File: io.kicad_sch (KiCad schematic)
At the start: 107 parts, among them CN1 DF40C-50DP-0.4V, J1 USB3_A, J13 WiFi SMA, J14 BLE SMA, J15 WiFi PATCH, J16 BLE PATCH, J17 BLE PATCH, J18 WIFI PATCH, U1 FUSB302BMPX, U12 PI3USB302-AZBEX, U13 VL817-Q7, U14 SiP32508DT, U15 TS5A23157DGSR, U16 AMLGA7921, U17 SiP32508DT, U30 PE4259-63, U36 PE4259-63, U37 2450CF15A0100001E, U38 X4C60K1-20S, U39 XEC24P3-30G, U40 AD8317ACPZ-R7, U41 AD8317ACPZ-R7, U42 AD8317ACPZ-R7, U43 LM339D, U7 HD3SS3220RNHR, Y2 25 MHz

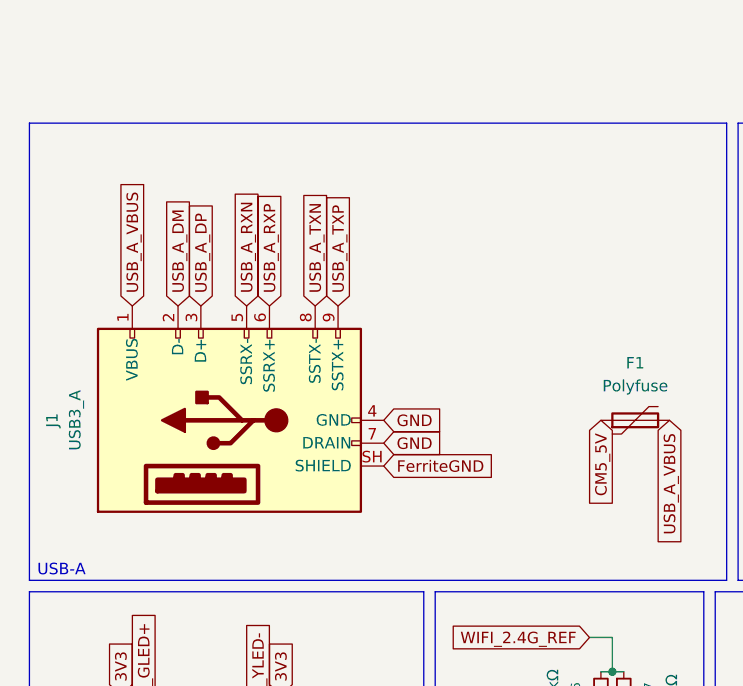
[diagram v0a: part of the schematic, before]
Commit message: assigned footprints and mpns across schematics + added 3d models and footprint libraries
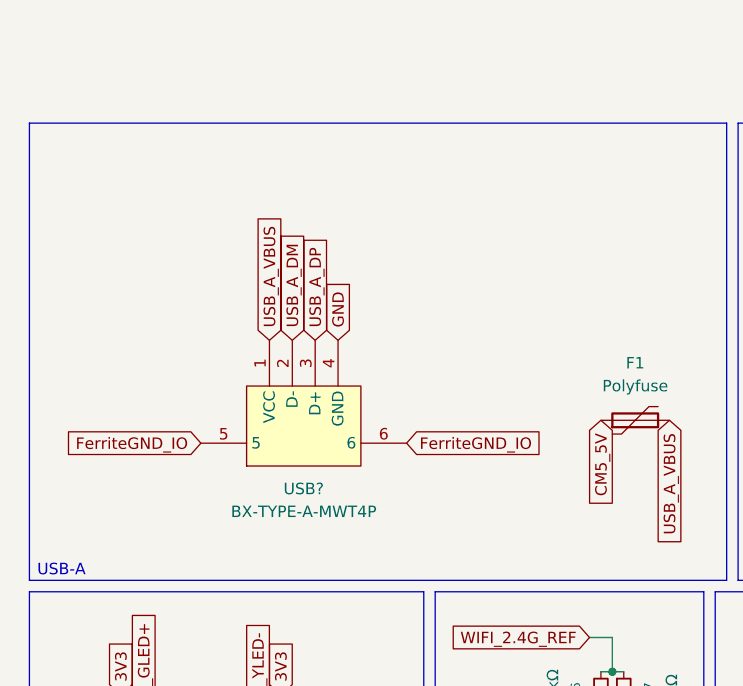
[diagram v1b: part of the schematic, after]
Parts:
- removed J1: USB3_A, slate113:HC-USB3_0-L168-WJ_COPY, symbol Connector:USB3_A
- added USB?: BX-TYPE-A-MWT4P, slate113:USB-A-SMD_BX-TYPE-A-MWT4P, symbol slate113:BX-TYPE-A-MWT4P
- U38: Manufacturer LCSC -> (none)
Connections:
- net FerriteGND_IO: now also USB?.5, USB?.6
- net GND: now also USB?.4 (GND)
- net USB_A_DM: now also USB?.2 (D-)
- net USB_A_DP: now also USB?.3 (D+)
- net USB_A_VBUS: now also USB?.1 (VCC)

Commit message: finished BOM, replaced discontinued parts, added missing footprints, updated schematics and libraries
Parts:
- C1, C106, C108, C22, C23, C24, C26, C27, C30, C31, C33, C36, C37, C38, C39, C40, C41, C43, C44, C45, C46, C47, C48, C49, C50, C51, C52, C53, C54, C55, C56: LCSC Part (none) -> C1591
- C100, C105, C107, C99: LCSC Part (none) -> C14858
- C101: footprint (none) -> Capacitor_SMD:C_0402_1005Metric; LCSC Part (none) -> C1546; MPN (none) -> 0402CG101J500NT
- C102, C93: footprint (none) -> Capacitor_SMD:C_0402_1005Metric; LCSC Part (none) -> C1579; MPN (none) -> 0402CG8R2C500NT
- C103: LCSC Part (none) -> C1579; MPN CL10C829JB8NNNC -> 0402CG8R2C500NT
- C104: footprint (none) -> Capacitor_SMD:C_0603_1608Metric; LCSC Part (none) -> C14858; MPN (none) -> CL10C101JB8NNNC
- C2: LCSC Part (none) -> C15849; MPN CL10B105KA8NNNC -> CL10A105KB8NNNC
- C32, C42: LCSC Part (none) -> C23630; MPN CL10B225KA8NNNC -> CL10A225KO8NNNC
- C34: LCSC Part (none) -> C380317; MPN CL10A106KP8NNNC -> TCC0603X5R106M160CT
- C94: footprint (none) -> Capacitor_SMD:C_0603_1608Metric; LCSC Part (none) -> C1591; MPN (none) -> CL10B104KB8NNNC
- F1: footprint Fuse:Fuse_1206_3216Metric -> Fuse:Fuse_0603_1608Metric; DigiKey Part (none) -> 13-SMD0603B050TFTR-ND; LCSC Part (none) -> C269155; MPN Littelfuse 1206L100/60YR -> SMD0603B050TF; Manufacturer DigiKey -> YAGEO
- FB3: footprint (none) -> Inductor_SMD:L_0603_1608Metric; LCSC Part (none) -> C107335; MPN (none) -> MPZ1608S601ATA00; Manufacturer (none) -> TDK
- J13: value WiFi SMA -> U.FL; footprint Connector_Coaxial:U.FL_Hirose_U.FL-R-SMT-1(10) -> slate113:IPEX-SMD_BWIPX-1-001E; LCSC Part (none) -> C496552; MPN Hirose U.FL-R-SMT-1(10) -> BWIPX-1-001E
- J14: value BLE SMA -> U.FL; footprint Connector_Coaxial:U.FL_Hirose_U.FL-R-SMT-1(10) -> slate113:IPEX-SMD_BWIPX-1-001E; LCSC Part (none) -> C496552; MPN Hirose U.FL-R-SMT-1(10) -> BWIPX-1-001E
- J15: value WiFi PATCH -> U.FL; footprint (none) -> slate113:IPEX-SMD_BWIPX-1-001E; LCSC Part (none) -> C496552; MPN Molex 1461870200 -> BWIPX-1-001E
- J16, J17: value BLE PATCH -> U.FL; footprint (none) -> slate113:IPEX-SMD_BWIPX-1-001E; LCSC Part (none) -> C496552; MPN Antenna Company AC11501-050UF -> BWIPX-1-001E
- J18: value WIFI PATCH -> U.FL; footprint (none) -> slate113:IPEX-SMD_BWIPX-1-001E; LCSC Part (none) -> C496552; MPN Molex 1461870200 -> BWIPX-1-001E
- L3: LCSC Part (none) -> C5378513; MPN Bourns SRP5030CA-4R7M -> FEXL0530A-4R7M
- R24, R25, R31, R32, R33, R36, R47, R50, R52, R53, R54, R55: LCSC Part (none) -> C25804; MPN RC0603FR-0710KL -> 0603WAF1002T5E
- R27, R3, R4: LCSC Part (none) -> C23162; MPN RC0603FR-074K7L -> 0603WAF4701T5E
- R28: LCSC Part (none) -> C22781; MPN RC0603FR-07110RL -> 0603WAF1100T5E
- R29: LCSC Part (none) -> C22787; MPN RC0603FR-07120RL -> 0603WAF1200T5E
- R34, R56, R58, R60: LCSC Part (none) -> C25803; MPN RC0603FR-07100KL -> 0603WAF1003T5E
- R35: LCSC Part (none) -> C22827; MPN RC0603FR-07180KL -> 0603WAF1803T5E
- R37: footprint (none) -> Resistor_SMD:R_0402_1005Metric; LCSC Part (none) -> C25913; MPN (none) -> 0402WGF6041TCE
- R45, R46: footprint (none) -> Resistor_SMD:R_0805_2012Metric; LCSC Part (none) -> C2828807; MPN (none) -> AR05DTBW0500
- R48, R49, R51: footprint (none) -> Resistor_SMD:R_0402_1005Metric; LCSC Part (none) -> C114978; MPN (none) -> 0402WGF523JTCE
- R57, R59, R61: LCSC Part (none) -> C4184; MPN RC0603FR-0720KL -> 0603WAF2002T5E
- U13: value VL817-Q7 -> GL3523-OTY3C; footprint slate113:QFN-76_L9.0-W9.0-P0.40-BL-EP -> (none); LCSC Part C209756 -> C19725282; MPN VL817-Q7(B0) -> GL3523-OTY3C; Manufacturer VIA Labs(威锋电子) -> Genesys Logic
- U14, U17: LCSC Part (none) -> C139515; MPN SiP32508DT -> SIP32508DT-T1-GE3
- U16: Manufacturer LCSC -> ALFA Network Inc.; Vendor Price (none) -> $24.97/unit (Rokland US, sold out at last check); no LCSC/D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
- U37: value 2450CF15A0100001E -> CPL0605AT13R2455A; DigiKey Part (none) -> 553-CPL0605AT13R2455ATR-ND; MPN 2450CF15A0100001E -> CPL0605AT13R2455A; Manufacturer LCSC -> Pulse Electronics
- U38: DigiKey Part (none) -> 1173-X4C60K1-20SRTR-ND; LCSC Part (none) -> C37211559; MPN X4C60K1-20S -> X4C60K1-20SR; Manufacturer (none) -> TTM Technologies, Inc.
- U39: DigiKey Part (none) -> 1173-XEC24P3-30GRTR-ND; MPN XEC24P3-30G -> XEC24P3-30GR; Manufacturer LCSC -> TTM Technologies, Inc.
- Y2: footprint (none) -> slate113:C5378513_IND-SMD_L5_5-W5_3; LCSC Part (none) -> C9006; MPN ECS-250-12-33Q-DS -> X322525MOB4SI
- gave numbers to parts that had none: 1

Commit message: imported footprints and 3d models, replaced obsolete components, finished schematic audit, wired new usb hub and flash chip + more, removed stale nets
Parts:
- removed L3: 4.7µH, symbol Device:L
- removed U13: GL3523-OTY3C, symbol slate113:VL817-Q7
- removed U39: XEC24P3-30G, symbol slate113:X4C60K1-20S
- removed Y2: 25 MHz, slate113:C5378513_IND-SMD_L5_5-W5_3, symbol Device:Crystal
- added C158, C159, C160, C161, C162, C163, C164, C212, C214, C218, C220, C221, C222, C223, C224, C225, C62: 100nF, symbol Device:C_Small
- added C165, C216, C61: 10µF, symbol Device:C_Small
- added C226, C227: 18pF, symbol Device:C_Small
- added C228: 2.2µF, Capacitor_SMD:C_0603_1608Metric, symbol Device:C_Small
- added C229: 100nF, Capacitor_SMD:C_0603_1608Metric, symbol Device:C_Small
- added L1: 4.7µH, symbol Device:L
- added R101: 20kΩ, symbol Device:R_Small
- added R102, R130, R131, R76: 10kΩ, symbol Device:R_Small
- added R103: 100kΩ, symbol Device:R_Small
- added R5: 100kΩ, Resistor_SMD:R_0603_1608Metric, symbol Device:R_Small
- added U13: W25Q32JVSSIQ, slate113:SOIC-8_L5.3-W5.3-P1.27-LS8.0-BL, symbol slate113:W25Q32JVSSIQ_C179173
- added U18: GL3523-OTY3C, slate113:QFN-76_L9.0-W9.0-P0.40-BL-EP5.8, symbol slate113:GL3523-OTY3C
- added U39: XEC24P3-30GR, symbol slate113:XEC24P3-30G
- added U53: SiP32508DT, Package_TO_SOT_SMD:TSOT-23-6, symbol Power_Management:SiP32508DT
- added U70: SkyLab WG243, symbol slate113:WG243
- added Y2: 25MHz, symbol Device:Crystal_Small
- C2: LCSC Part C15849 -> C92848; MPN CL10A105KB8NNNC -> UMK107BJ105KA-T; Manufacturer Samsung Electro-Mechanics -> Taiyo Yuden
- C34: value 10µF -> 100nF; footprint Capacitor_SMD:C_0603_1608Metric -> (none); LCSC Part C380317 -> (none); MPN TCC0603X5R106M160CT -> (none); Manufacturer Samsung Electro-Mechanics -> (none)
- R24, R47, R50, R52, R53, R54, R55: LCSC Part C25804 -> C840630; MPN 0603WAF1002T5E -> CR0603-FX-1002ELF; Manufacturer Yageo -> Bourns
- R25, R31, R32, R33, R36: footprint Resistor_SMD:R_0603_1608Metric -> (none); LCSC Part C25804 -> (none); MPN 0603WAF1002T5E -> (none); Manufacturer Yageo -> (none)
- R27, R3, R4: LCSC Part C23162 -> C163914; MPN 0603WAF4701T5E -> WR06X4701FTL; Manufacturer Yageo -> Walsin
- R28: LCSC Part C22781 -> C217696; MPN 0603WAF1100T5E -> ARG03FTC1100; Manufacturer Yageo -> Viking Tech
- R35: LCSC Part C22827 -> C123419; MPN 0603WAF1803T5E -> RC0603FR-07180KL
- R37: value 6.04kΩ ±1% -> 10kΩ; footprint Resistor_SMD:R_0402_1005Metric -> (none); LCSC Part C25913 -> (none); MPN 0402WGF6041TCE -> (none)
- R57, R59, R61: LCSC Part C4184 -> C844923; MPN 0603WAF2002T5E -> CRCW060320K0FKEA; Manufacturer Yageo -> Vishay Dale
- U30, U36: DigiKey Part (none) -> 1046-1011-1-ND
- U37: footprint (none) -> slate113:CPL0605AT13R2455A
- U38: value X4C60K1-20S -> X4C60K1-20SR; footprint (none) -> slate113:X4C60K1-20S; LCSC Part C37211559 -> (none); RFMW Part (none) -> 711055
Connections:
- net 2.4G_SENSE: now also R53.2, R54.2, U43.1, U43.2; no longer C1.1, C105.1, C106.1, C107.1, C108.1, C2.1, C22.2, C23.2, C24.2, C30.1, C41.1, C42.1, C94.1, C99.1, CN1.49, CN1.6, CN1.7, R24.1, R25.2, R27.1, R28.1, R29.1, R3.1, R31.2, R32.2, R33.2, R36.2, R4.1, R53.1, R54.1, R55.1, R56.1, R58.1, R60.1, U12.1 (VDD), U12.10 (VDD), U12.6 (VDD), U15.8 (V+), U30.6 (CTRL#orVDD), U36.6 (CTRL#orVDD), U40.7 (VPOS), U41.7 (VPOS), U42.7 (VPOS), U43.10, U43.3 (VDD)
- net BLE_ANT1: now also U70.12 (BT)
- net BLE_CPL: now also U37.4 (Coupled_Out); no longer U37.5 (Coupled_Out)
- net BLE_SMA_ANT: now also U37.3 (Output); no longer U37.8 (Output)
- net BLE_SW_SMA: now also U37.2 (Input); no longer U37.4 (Input)
- net CM5_5V: now also C228.1
- net GND: now also C34.2, C158.2, C159.2, C160.2, C161.2, C162.2, C163.2, C164.2, C165.2, C212.2, C214.2, C216.2, C218.2, C220.2, C221.2, C222.2, C223.2, C224.2, C225.2, C226.1, C227.2, C61.1, C62.1, R101.1, R103.2, R5.2, U13.4 (GND), U18.40 (VSSP), U18.77 (EP), U53.4 (GND), U70.1 (GND), U70.10 (GND), U70.11 (GND), U70.13 (GND), U70.23 (GND), U70.25 (GND), U70.28 (GND), U70.3 (GND), U70.31 (GND), U70.34 (GND), U70.37 (GND), U70.39 (GND), U70.4 (GND), U70.46 (GND), U70.48 (GND), U70.5 (GND), U70.6 (GND), U70.7 (GND), U70.8 (GND); no longer C34.1, R37.2, U37.2 (GND), U37.3 (GND), U37.6 (GND), U37.7 (GND)
- net M2_DM: now also U18.14 (DM_P3)
- net M2_DP: now also U18.13 (DP_P3)
- net M2_EN: now also U18.33 (PWREN3J)
- net USB1_DN: now also U18.26 (DM_P2)
- net USB1_DP: now also U18.25 (DP_P2)
- net USB1_PWREN: now also U18.36 (PWREN2J)
- net USB2_H_DM: now also U18.67 (DM_P0)
- net USB2_H_DP: now also U18.66 (DP_P0)
- net USB_A_DM: now also U18.64 (DM_P1)
- net USB_A_DP: now also U18.63 (DP_P1)
- net USB_HUB_RST: now also R76.2, U18.48 (RESETJ)
- net WIFI_2.4G_5G: now also U39.2 (Direct)
- net WIFI_2.4G_CPL: now also U39.4 (Coupled)
- net WIFI_2.4G_ISO: now also U39.3 (Isolated)
- net WIFI_ANT0: now also U70.9 (S0)
- net WIFI_ANT1: now also U70.2 (S1)
- net WIFI_CAPS: now also C61.2, C62.2, R130.2, R131.2, U70.36 (VD33)
- net WIFI_DM: now also U18.11 (DM_P4), U70.33 (HSDM)
- net WIFI_DP: now also U18.10 (DP_P4), U70.32 (HSDP)
- net WIFI_PWREN: now also U18.32 (PWREN4J)
- net WIFI_SW_SMA: now also U39.1 (Input)
- net WOWLAN: now also CN1.21, U70.16 (WL_WAKE_HOST); no longer U16.10 (#WOWLAN)
- net 3V3: now reaches R31.1
- net 3V3: now also C1.1, C105.1, C106.1, C107.1, C108.1, C2.1, C22.2, C23.2, C24.2, C30.1, C34.1, C41.1, C42.1, C94.1, C99.1, CN1.6, CN1.7, R24.1, R25.1, R27.1, R28.1, R29.1, R3.1, R32.1, R33.1, R36.1, R37.1, R4.1, R53.1, R54.1, R55.1, R56.1, R58.1, R60.1, U12.1 (VDD), U12.10 (VDD), U12.6 (VDD), U15.8 (V+), U30.6 (CTRL#orVDD), U36.6 (CTRL#orVDD), U40.7 (VPOS), U41.7 (VPOS), U42.7 (VPOS), U43.10, U43.3 (VDD), C158.1, C159.1, C160.1, C161.1, C225.1, R102.1, R76.1, U13.8 (VCC), U18.12 (AVDD33_2), U18.27 (AVDD33_3), U18.44 (V33), U18.55 (DVDD33), U18.65 (AVDD33_1), U18.73 (AVDD33)
- net USB_HUB_EN: now reaches CN1.18
- net USB_HUB_EN: now also U53.3 (EN)
- net BT_EN: now reaches CN1.19
- net BT_EN: now also R131.1, U70.38 (BT_DISn)
- net WIFI_EN: now reaches CN1.20
- net WIFI_EN: now also R130.1, U70.15 (WL_DISn)
- net COMBO_EN: now reaches CN1.22
- net COMBO_EN: now also U70.24 (RESET)
- net BLE_SENSE: now reaches R55.2, U43.14
- net BLE_SENSE: now also CN1.49
- net at U37.1 (Terminiation): now also R5.1
- net USB1_SS_RXN: no longer names the net of U12.16 (Rx1-)
- net USB1_SS_RXP: no longer names the net of U12.17 (Rx1+)
- net USB1_SS_TXN: no longer names the net of U12.18 (Tx1-)
- net USB1_SS_TXP: no longer names the net of U12.19 (Tx1+)
- net WIFI_RXN: no longer names the net of U16.4 (SSUSB_RXN)
- net WIFI_RXP: no longer names the net of U16.5 (SSUSB_RXP)
- net WIFI_TXN: no longer names the net of U16.1 (SSUSB_TXN)
- net WIFI_TXP: no longer names the net of U16.2 (SSUSB_TXP)
- new net: R103.1, U18.53 (PGANG)
- new net: R25.2, U13.3 (WP#(IO2))
- new net: R31.2, U13.7 (HOLD#/RESET#/IO3)
- new net: R37.2, U18.31 (OVCUR4J/SMD)
- new net: R101.2, U18.46 (RTERM)
- new net: R36.2, U18.34 (OVCUR3J/SMC)
- new net: L1.2, U18.41 (SW)
- new net: C228.2, U53.5 (IN), U53.6 (IN)
- new net: C229.2, U53.1 (OUT), U53.2 (OUT)
- new net: R102.2, U18.45 (CHIPEN)
- new net: R33.2, U18.35 (OVCUR2J)
- new net: C227.1, U18.56 (X2), Y2.1
- new net: C226.2, U18.57 (X1), Y2.2
- new net: R32.2, U18.38 (OVCUR1J)
- new net HUB_1V2: C162.1, C163.1, C164.1, C165.1, C220.1, C221.1, C222.1, C223.1, C224.1, L1.1, U18.17 (VP12_P3), U18.22 (VP12_P2), U18.28 (DVDD12), U18.39 (FB), U18.4 (AVDD12), U18.47 (DVDD12), U18.60 (VP12_P1), U18.7 (VP12_P4), U18.70 (VP12_P0)
- new net HUB_5V: C212.1, C214.1, C216.1, C218.1, C229.1, U18.42 (VDDP), U18.43 (V5), U18.54 (VBUS)
- new net HUB_CLK: U13.6 (CLK), U18.50 (P_SPI_CK)
- new net HUB_CS#: U13.1 (~{CS}), U18.52 (P_SPI_CZ)
- new net HUB_DI: U13.5 (DI(IO0)), U18.51 (P_SPI_DI)
- new net HUB_DO: U13.2 (DO(IO1)), U18.49 (P_SPI_DO)
- no-connect marks 32 -> 72
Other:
- note added: "Hub Caps"
- note added: "Hub Flash"
- note added: "USB Hub Power"
- moved on the sheet: C1, C100, C101, C102, C103, C104, C105, C106, C107, C108, C2, C22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

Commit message: configured 8-layer pcb with micro vias, finished power mezzanine routing, completed io port, started work on slateconnect mezzanine
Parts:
- removed R24: 10kΩ, Resistor_SMD:R_0603_1608Metric, symbol Device:R_Small
- removed U16: AMLGA7921, symbol slate113:AMLGA7921
- removed Y2: 25MHz, symbol Device:Crystal_Small
- added X1: X322525MOB4SI, slate113:CRYSTAL-SMD_4P-L3.2-W2.5-BL_X322525MOB4SI, symbol slate113:X322525MOB4SI
- C158, C162: footprint (none) -> Capacitor_SMD:C_0603_1608Metric; LCSC Part (none) -> C1591; MPN (none) -> CL10B104KB8NNNC; Manufacturer (none) -> Samsung Electro-Mechanics
- C159, C160, C161, C163, C164, C212, C214, C218, C220, C221, C222, C223, C224, C225, C34, C62: footprint (none) -> Capacitor_SMD:C_0603_1608Metric; LCSC Part (none) -> C1591; MPN (none) -> CL10B104KB8NNNC; Manufacturer (none) -> Samsung
- C165, C216, C61: footprint (none) -> Capacitor_SMD:C_0603_1608Metric; LCSC Part (none) -> C380317; MPN (none) -> TCC0603X5R106M160CT; Manufacturer (none) -> CCTC
- C226: footprint (none) -> Capacitor_SMD:C_0402_1005Metric
- C227: footprint (none) -> Capacitor_SMD:C_0402_1005Metric; LCSC Part (none) -> C106202; MPN (none) -> CC0402JRNPO9BN180; Manufacturer (none) -> Yageo
- L1: footprint (none) -> slate113:IND-SMD_L5.5-W5.3
- R101: footprint (none) -> Resistor_SMD:R_0603_1608Metric; LCSC Part (none) -> C844923; MPN (none) -> CRCW060320K0FKEA; Manufacturer (none) -> Vishay
- R102, R130, R131, R25, R31, R32, R33, R36, R37, R76: footprint (none) -> Resistor_SMD:R_0603_1608Metric; LCSC Part (none) -> C25804; MPN (none) -> 0603WAF1002T5E; Manufacturer (none) -> UNI-ROYAL
- R103: footprint (none) -> Resistor_SMD:R_0603_1608Metric; LCSC Part (none) -> C25803; MPN (none) -> 0603WAF1003T5E; Manufacturer (none) -> UNI-ROYAL
- U39: footprint (none) -> slate113:XEC24P3-30G
- U70: footprint (none) -> slate113:WG243
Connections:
- net GND: now also X1.2 (GND), X1.4 (GND)
- net at C227.1, U18.56 (X2): now also X1.3 (OSC2)
- net at C226.2, U18.57 (X1): now also X1.1 (OSC1)
- no-connect marks 72 -> 68
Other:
- moved on the sheet: C226
